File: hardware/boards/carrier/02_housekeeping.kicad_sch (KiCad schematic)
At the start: 15 parts, among them U1 STM32G031G6U6

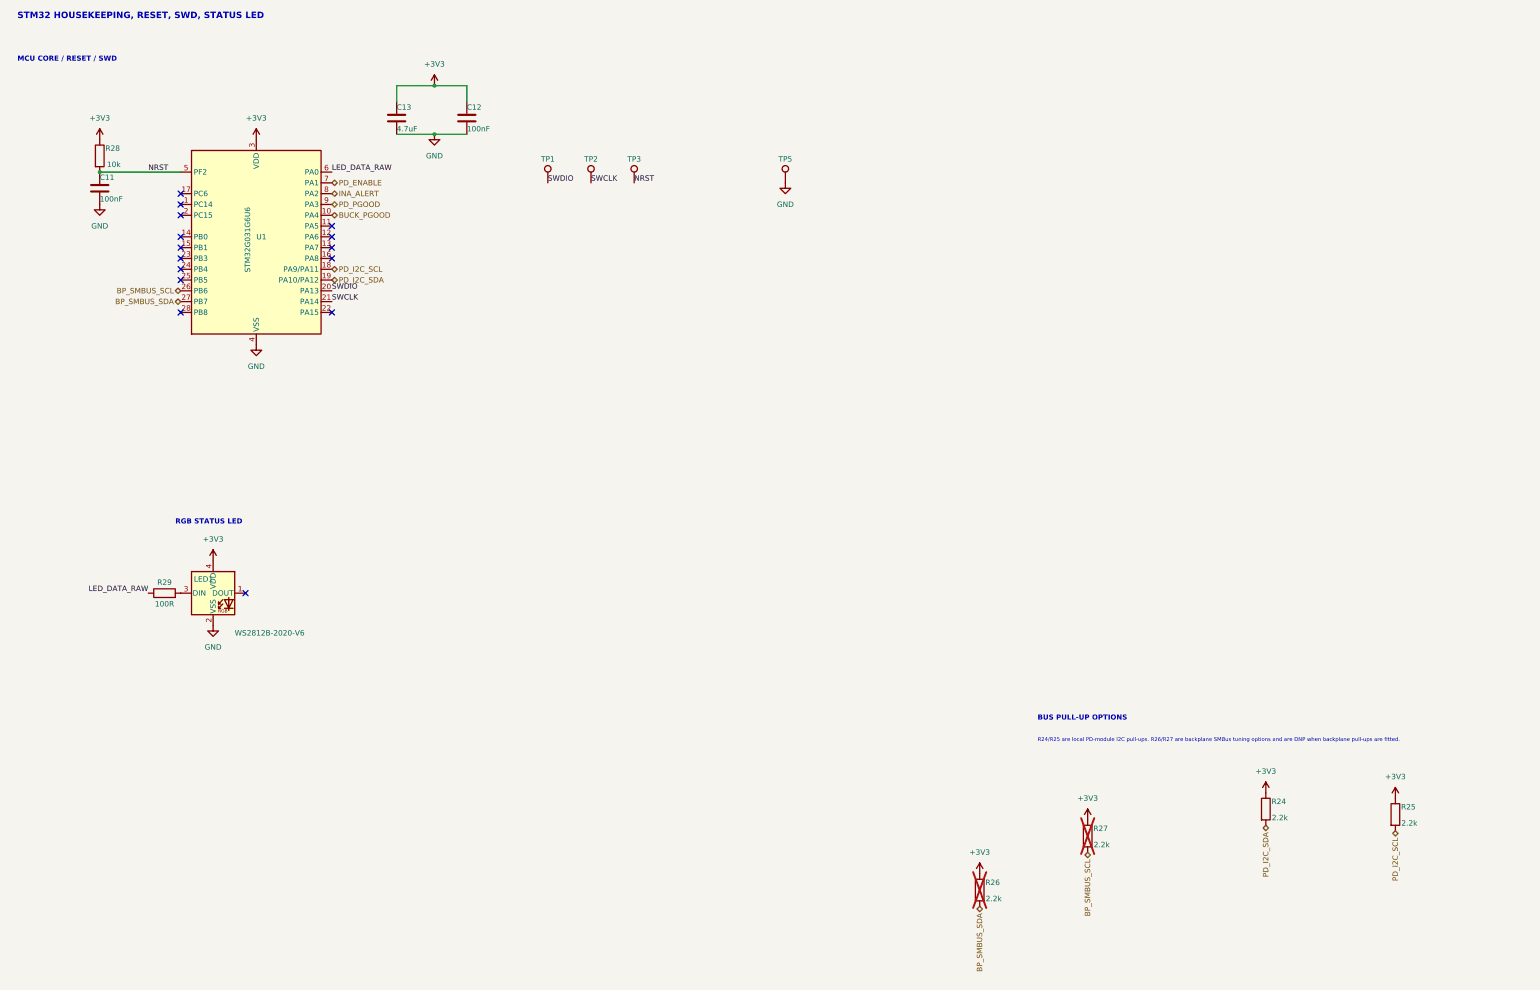
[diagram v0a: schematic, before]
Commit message: checkpoint: carrier schematic edits and SW3538 references
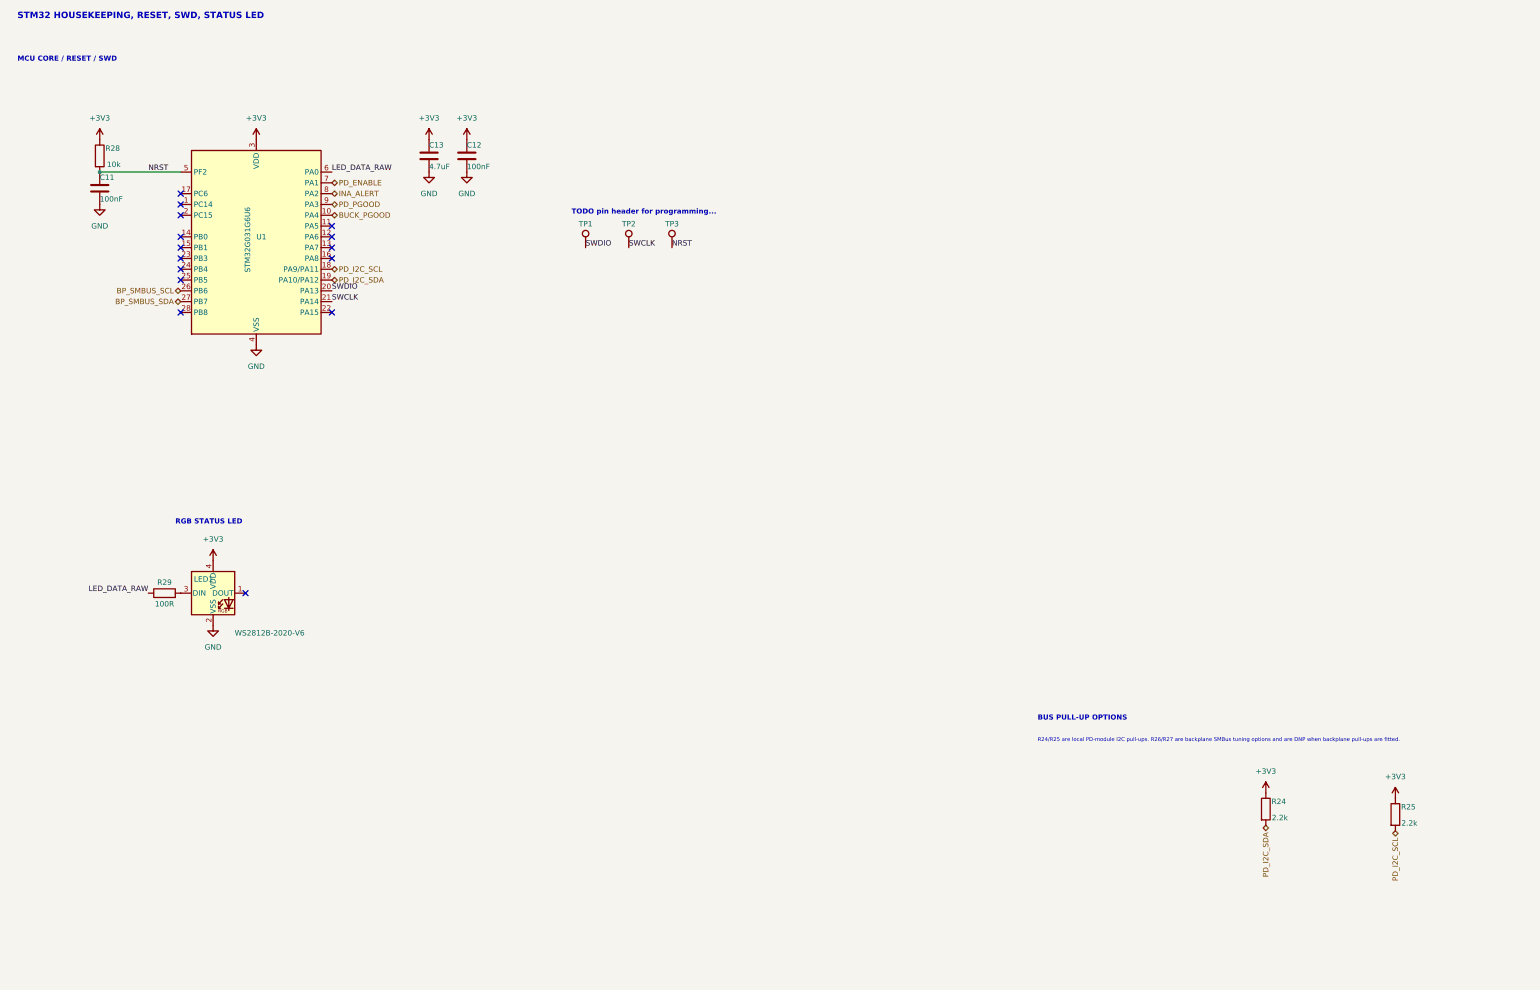
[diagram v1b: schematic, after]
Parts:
- removed R26, R27: 2.2k, Resistor_SMD:R_0603_1608Metric, symbol Device:R
- removed TP5: GND, TestPoint:TestPoint_Pad_D1.0mm, symbol Connector:TestPoint
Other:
- note added: "TODO pin header for programming..."
- moved on the sheet: C12, C13, TP1, TP2, TP3

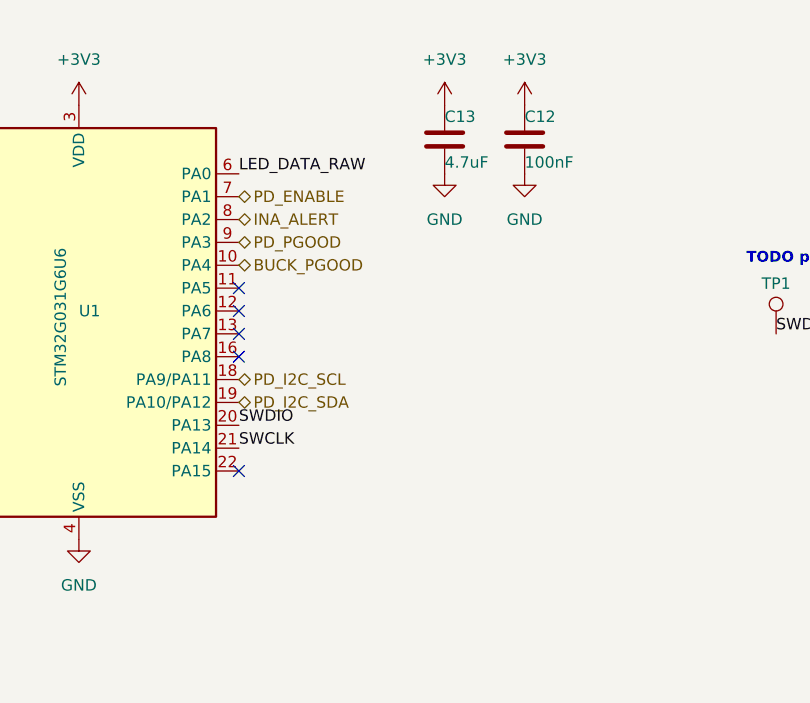
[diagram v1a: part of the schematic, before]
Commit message: hardware: route SW3538 IRQ to carrier MCU
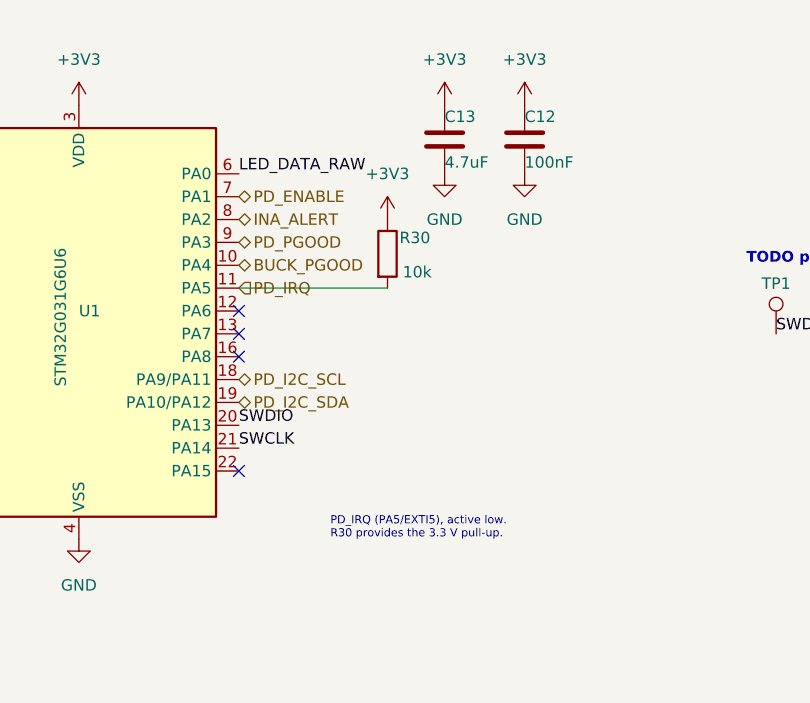
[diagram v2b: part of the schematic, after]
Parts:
- added R30: 10k, Resistor_SMD:R_0603_1608Metric, symbol Device:R
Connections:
- net +3V3: now also R30.1
- net PD_IRQ: now reaches U1.11 (PA5)
- net PD_IRQ: now also R30.2
- no-connect marks 15 -> 14
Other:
- note added: "PD_IRQ (PA5/EXTI5), active low. R30 provides the 3.3 V pull-up."
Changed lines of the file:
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@@
+		)
+	)
+	(text "PD_IRQ (PA5/EXTI5), active low.\nR30 provides the 3.3 V pull-up."
+		(exclude_from_sim no)
+		(at 104.14 91.44 0)
+		(effects
+			(font
+				(size 0.9 0.9)
+			)
+			(justify left bottom)
 		)
 	)
@@
 	)
 	(no_connect
-		(at 93.98 63.5)
-	)
-	(no_connect
 		(at 58.42 73.66)
 	)
@@
 		)
 	)
+	(wire
+		(pts
+			(xy 93.98 63.5) (xy 110.49 63.5)
+		)
+		(stroke
+			(width 0)
+			(type default)
+		)
+	)
 	(label "SWCLK"
 		(at 163.83 68.58 0)
@@
 		)
 	)
+	(hierarchical_label "PD_IRQ"
+		(shape input)
+		(at 93.98 63.5 0)
+		(effects
+			(font
+				(size 1.27 1.27)
+			)
+			(justify left bottom)
+		)
+	)
+	(symbol
+		(lib_id "power:+3V3")
+		(at 110.49 55.88 0)
+		(unit 1)
+		(body_style 1)
+		(exclude_from_sim no)
+		(in_bom yes)
+		(on_board yes)
+		(in_pos_files yes)
+		(dnp no)
+		(fields_autoplaced yes)
+		(property "Reference" "#PWR67"
+			(at 110.49 59.69 0)
+			(hide yes)
+			(show_name no)
+			(do_not_autoplace no)
+			(effects
+				(font
+					(size 1.27 1.27)
+				)
+			)
+		)
+		(property "Value" "+3V3"
+			(at 110.49 50.8 0)
+			(show_name no)
+			(do_not_autoplace no)
+			(effects
+				(font
+					(size 1.27 1.27)
+				)
+			)
+		)
+		(property "Footprint" ""
+			(at 110.49 55.88 0)
+			(hide yes)
+			(show_name no)
+			(do_not_autoplace no)
+			(effects
+				(font
+					(size 1.27 1.27)
+				)
+			)
+		)
+		(property "Datasheet" ""
+			(at 110.49 55.88 0)
+			(hide yes)
+			(show_name no)
+			(do_not_autoplace no)
+			(effects
+				(font
+					(size 1.27 1.27)
+				)
+			)
+		)
+		(property "Description" "Power symbol creates a global label with name \"+3V3\""
+			(at 110.49 55.88 0)
+			(hide yes)
+			(show_name no)
+			(do_not_autoplace no)
+			(effects
+				(font
+					(size 1.27 1.27)
+				)
+			)
+		)
+		(pin "1"
+		)
+		(instances
+			(project "carrier"
+				(path "/ee42a069-09cc-4091-bee3-2dd6ab96c98c/64ed744c-f0e1-4d20-9137-f6a463447101"
+					(reference "#PWR67")
+					(unit 1)
+				)
+			)
+		)
+	)
+	(symbol
+		(lib_id "Device:R")
+		(at 110.49 59.69 0)
+		(unit 1)
+		(body_style 1)
+		(exclude_from_sim no)
+		(in_bom yes)
+		(on_board yes)
+		(in_pos_files yes)
+		(dnp no)
+		(property "Reference" "R30"
+			(at 113.538 57.912 0)
+			(show_name no)
+			(do_not_autoplace no)
+			(effects
+				(font
+					(size 1.27 1.27)
+				)
+			)
+		)
+		(property "Value" "10k"
+			(at 113.792 61.722 0)
+			(show_name no)
+			(do_not_autoplace no)
+			(effects
+				(font
+					(size 1.27 1.27)
+				)
+			)
+		)
+		(property "Footprint" "Resistor_SMD:R_0603_1608Metric"
+			(at 108.712 59.69 90)
+			(hide yes)
+			(show_name no)
+			(do_not_autoplace no)
+			(effects
+				(font
+					(size 1.27 1.27)
+				)
+			)
+		)
+		(property "Datasheet" ""
+			(at 110.49 59.69 0)
+			(hide yes)
+			(show_name no)
+			(do_not_autoplace no)
+			(effects
+				(font
+					(size 1.27 1.27)
+				)
+			)
+		)
+		(property "Description" "Resistor"
+			(at 110.49 59.69 0)
+			(hide yes)
+			(show_name no)
+			(do_not_autoplace no)
+			(effects
+				(font
+					(size 1.27 1.27)
+				)
+			)
+		)
+		(pin "1"
+		)
+		(pin "2"
+		)
+		(instances
+			(project "carrier"
+				(path "/ee42a069-09cc-4091-bee3-2dd6ab96c98c/64ed744c-f0e1-4d20-9137-f6a463447101"
+					(reference "R30")
+					(unit 1)
+				)
+			)
+		)
+	)

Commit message: checkpoint: carrier schematic readability edits
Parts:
- removed TP1: SWDIO, TestPoint:TestPoint_Pad_D1.0mm, symbol Connector:TestPoint
- removed TP2: SWCLK, TestPoint:TestPoint_Pad_D1.0mm, symbol Connector:TestPoint
- removed TP3: NRST, TestPoint:TestPoint_Pad_D1.0mm, symbol Connector:TestPoint
- added J2: (no value), symbol Connector:Conn_01x05_Pin
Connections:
- net +3V3: now also J2.2 (Pin_2)
- net GND: now also J2.1 (Pin_1)
- net NRST: now also J2.3 (Pin_3)
- net SWCLK: now also J2.4 (Pin_4)
- net SWDIO: now also J2.5 (Pin_5)
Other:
- note added: "Pin header for programming"
- note removed: "TODO pin header for programming..."
- moved on the sheet: C12, C13, R30

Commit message: hardware: fix carrier buck status and programming header
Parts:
- J2: footprint (none) -> Connector_PinHeader_2.54mm:PinHeader_1x05_P2.54mm_Vertical
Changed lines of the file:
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@@
 			)
 		)
-		(property "Footprint" ""
+		(property "Footprint" "Connector_PinHeader_2.54mm:PinHeader_1x05_P2.54mm_Vertical"
 			(at 179.07 85.09 0)
 			(hide yes)

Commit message: checkpoint: carrier layout edits
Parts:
- removed R29: 100R, Resistor_SMD:R_0603_1608Metric, symbol Device:R
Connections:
- net LED_DATA_RAW: now also LED1.3 (DIN)
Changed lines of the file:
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@@
 	)
 	(label "LED_DATA_RAW"
-		(at 50.8 149.86 180)
+		(at 58.42 149.86 180)
 		(effects
 			(font
@@
 					(unit 1)
 				)
-			)
-		)
-	)
-	(symbol
-		(lib_id "Device:R")
-		(at 54.61 149.86 90)
-		(unit 1)
-		(body_style 1)
-		(exclude_from_sim no)
-		(in_bom yes)
-		(on_board yes)
-		(in_pos_files yes)
-		(dnp no)
-		(property "Reference" "R29"
-			(at 54.61 147.32 90)
-			(show_name no)
-			(do_not_autoplace no)
-			(effects
-				(font
-					(size 1.27 1.27)
-				)
-			)
-		)
-		(property "Value" "100R"
-			(at 54.61 152.4 90)
-			(show_name no)
-			(do_not_autoplace no)
-			(effects
-				(font
-					(size 1.27 1.27)
-				)
-			)
-		)
-		(property "Footprint" "Resistor_SMD:R_0603_1608Metric"
-			(at 54.61 151.638 90)
-			(hide yes)
-			(show_name no)
-			(do_not_autoplace no)
-			(effects
-				(font
-					(size 1.27 1.27)
-				)
-			)
-		)
-		(property "Datasheet" ""
-			(at 54.61 149.86 0)
-			(hide yes)
-			(show_name no)
-			(do_not_autoplace no)
-			(effects
-				(font
-					(size 1.27 1.27)
-				)
-			)
-		)
-		(property "Description" "Resistor"
-			(at 54.61 149.86 0)
-			(hide yes)
-			(show_name no)
-			(do_not_autoplace no)
-			(effects
-				(font
-					(size 1.27 1.27)
-				)
-			)
-		)
-		(pin "1"
-		)
-		(pin "2"
-		)
-		(instances
-			(project "carrier"
-				(path "/ee42a069-09cc-4091-bee3-2dd6ab96c98c/64ed744c-f0e1-4d20-9137-f6a463447101"
-					(reference "R29")
-					(unit 1)
-				)

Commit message: hardware: prepare carrier mechanics and assembly
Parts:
- J2: now not fitted
- LED1: value WS2812B-2020-V6 -> WS2812B-4020-V6; footprint LED_SMD:LED_WS2812B-2020_PLCC4_2.0x2.0mm -> mini-rack-power:LED_Worldsemi_WS2812B-4020_SideView; symbol LED:WS2812B-2020 -> mini-rack-power:WS2812B-4020-V6; LCSC C52917434 -> C52941387; MPN WS2812B-2020-V6 -> WS2812B-4020-V6
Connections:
- net +3V3: now also LED1.2 (VDD); no longer LED1.4 (VDD)
- net GND: now also LED1.4 (VSS); no longer LED1.2 (VSS)
- net LED_DATA_RAW: now also LED1.1 (DIN); no longer LED1.3 (DIN)
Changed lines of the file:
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@@
 		(in_bom yes)
 		(on_board yes)
-		(in_pos_files yes)
-		(dnp no)
+		(in_pos_files no)
+		(dnp yes)
 		(fields_autoplaced yes)
 		(property "Reference" "J2"
@@
 	)
 	(symbol
-		(lib_id "LED:WS2812B-2020")
+		(lib_id "mini-rack-power:WS2812B-4020-V6")
 		(at 66.04 149.86 0)
 		(unit 1)
@@
 			)
 		)
-		(property "Value" "WS2812B-2020-V6"
+		(property "Value" "WS2812B-4020-V6"
 			(at 71.12 158.496 0)
 			(show_name no)
@@
 			)
 		)
-		(property "Footprint" "LED_SMD:LED_WS2812B-2020_PLCC4_2.0x2.0mm"
+		(property "Footprint" "mini-rack-power:LED_Worldsemi_WS2812B-4020_SideView"
 			(at 67.31 142.24 0)
 			(hide yes)
@@
 			)
 		)
-		(property "Datasheet" "https://cdn-shop.adafruit.com/product-files/4684/4684_WS2812B-2020_V1.3_EN.pdf"
+		(property "Datasheet" "https://datasheet.lcsc.com/datasheet/pdf/ec5ab06f6bef843823cdd508ed36b03e.pdf?productCode=C52941387"
 			(at 68.58 140.335 0)
 			(hide yes)
@@
 			)
 		)
-		(property "Description" "RGB LED with integrated controller, 2.0 x 2.0 mm, 12 mA"
+		(property "Description" "Side-view RGB LED with integrated WS2812-compatible controller, 3.3 V capable, 3.98 x 2.00 x 1.70 mm"
 			(at 66.04 149.86 0)
 			(hide yes)
@@
 			)
 		)
-		(property "MPN" "WS2812B-2020-V6"
+		(property "MPN" "WS2812B-4020-V6"
 			(at 66.04 149.86 0)
 			(hide yes)
@@
 			)
 		)
-		(property "LCSC" "C52917434"
+		(property "LCSC" "C52941387"
 			(at 66.04 149.86 0)
 			(hide yes)

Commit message: hardware: refine carrier power placement and LED fallback
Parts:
- LED1: Alternate_LCSC (none) -> C52917434; Alternate_MPN (none) -> WS2812B-2020-V6; Population_Note (none) -> Populate either the 4020 side-view pads or the 2020 top-emi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
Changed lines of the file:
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@@
+			)
+		)
+		(property "Alternate_MPN" "WS2812B-2020-V6"
+			(at 66.04 149.86 0)
+			(hide yes)
+			(show_name no)
+			(do_not_autoplace no)
+			(effects
+				(font
+					(size 1.27 1.27)
+				)
+			)
+		)
+		(property "Alternate_LCSC" "C52917434"
+			(at 66.04 149.86 0)
+			(hide yes)
+			(show_name no)
+			(do_not_autoplace no)
+			(effects
+				(font
+					(size 1.27 1.27)
+				)
+			)
+		)
+		(property "Population_Note" "Populate either the 4020 side-view pads or the 2020 top-emitting pads, never both"
+			(at 66.04 149.86 0)
+			(hide yes)
+			(show_name no)
+			(do_not_autoplace no)
+			(effects
+				(font
+					(size 1.27 1.27)
+				)
 			)
 		)
